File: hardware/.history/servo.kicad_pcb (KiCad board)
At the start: 2 copper layers, 45 x 43 mm, 37 parts, among them J1 servo, J2 Jack-DC, J3 swd, Q2 DMT64M8LSS, SW1 restart, SW2 buzzer, U1 AOZ1284PI, U3 STM32G030F6Px, U4 LDI1117-3.3U-DIO

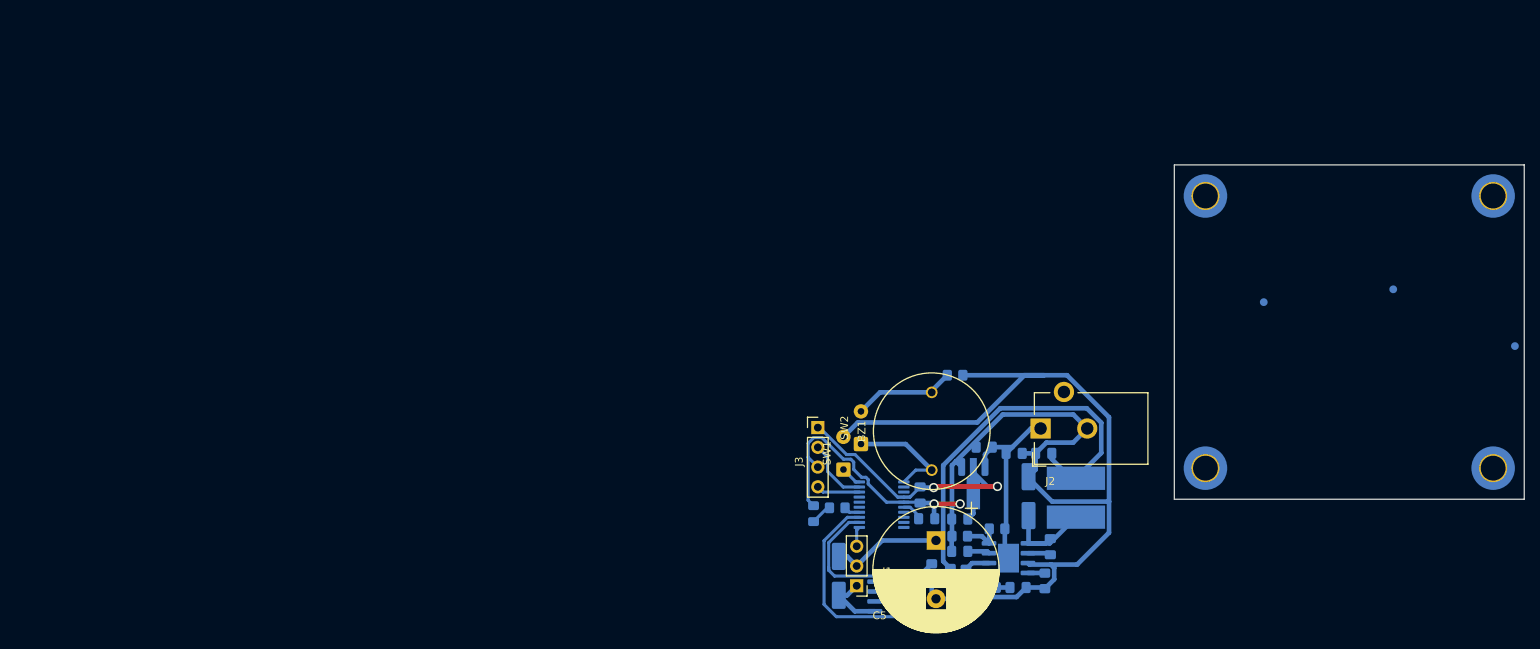
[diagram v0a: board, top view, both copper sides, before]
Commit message: Fix false stall detection after restart
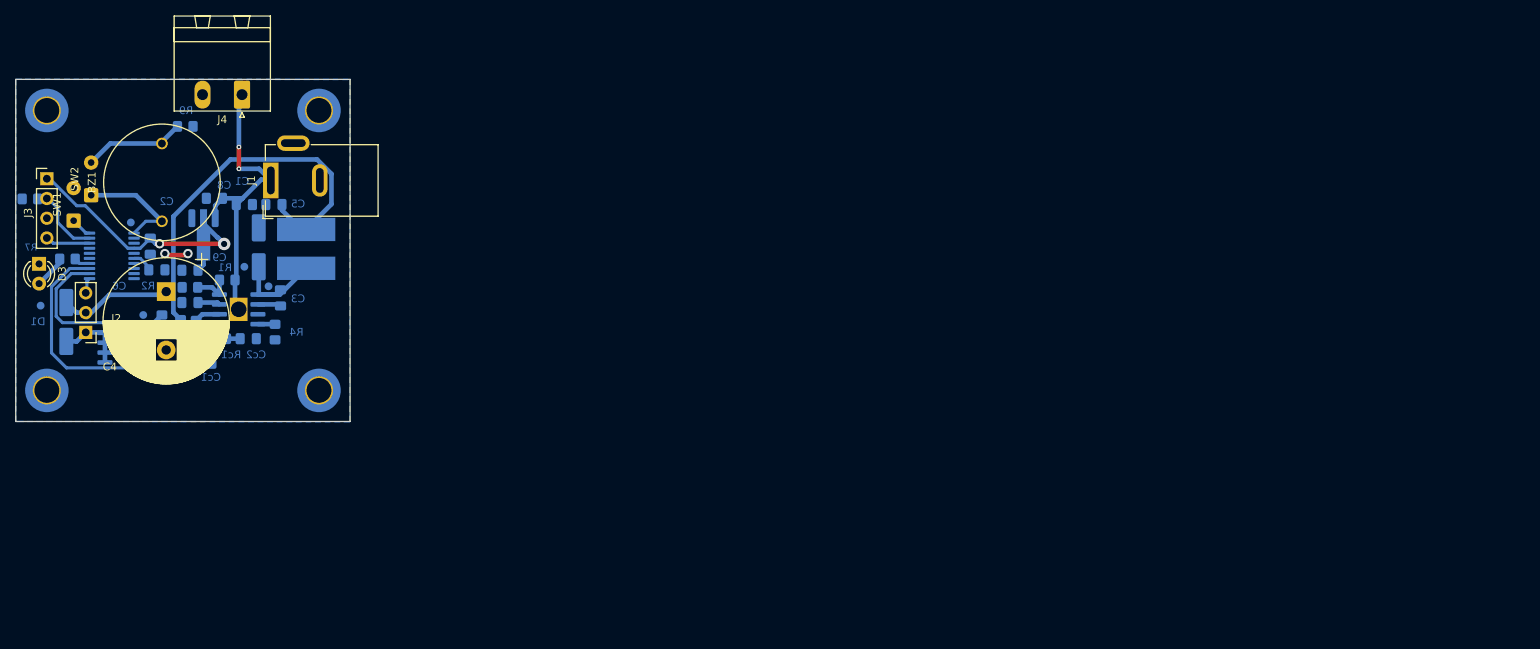
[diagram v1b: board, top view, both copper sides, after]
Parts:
- added Cc1: 150p, Capacitor_SMD:C_0805_2012Metric_Pad1.18x1.45mm_HandSolder, B.Cu at (25.1, 35.6)
- added J4: LED, Connector_Phoenix_MSTB:PhoenixContact_MSTBA_2,5_2-G-5,08_1x02_P5.08mm_Horizontal, F.Cu at (29.1, 1.96)
- added R8: 10k, Resistor_SMD:R_0805_2012Metric_Pad1.20x1.40mm_HandSolder, B.Cu at (1.82, 15.4)
- C7: renamed from C4; value 220n -> 220n 10V
- C8: renamed from C7; value 1u 25V -> 1u 16V
- Cc2: renamed from C6; value 1.5n -> 6.8n
- D3: value KP-2012SURC -> L-7104SURCK; footprint LED_SMD:LED_0805_2012Metric_Pad1.15x1.40mm_HandSolder -> LED_THT:LED_D3.0mm; moved to F.Cu
- J1: renamed from J2; value Jack-DC -> 5.5x2.1; footprint Connector_BarrelJack:BarrelJack_CUI_PJ-102AH_Horizontal -> Connector_BarrelJack:BarrelJack_GCT_DCJ200-10-A_Horizontal
- R9: renamed from R7; value 51k -> 300
- Rc1: renamed from R4; value 10k -> 1M
- U1: footprint Package_SO:SOIC-8-1EP_3.9x4.9mm_P1.27mm_EP2.71x3.7mm -> Package_SO:SOIC-8-1EP_3.9x4.9mm_P1.27mm_EP2.29x3mm_diy
- moved H3 186.3 mm to (4.00, 40.0)
- moved H1 153.1 mm to (39.0, 40.0)
- moved H2 149.4 mm to (4.00, 4.00)
- moved H4 122.9 mm to (39.0, 4.00)
- moved D3 104.7 mm to (3.00, 23.7)
- moved D1 104.6 mm to (6.50, 31.2)
- moved J2 104.4 mm to (9.00, 32.5)
- moved J3 104.2 mm to (4.00, 12.8)
- moved C3 104.0 mm to (34.0, 28.1)
- moved R7 104.0 mm to (6.65, 23.1)
- moved BZ1 104.0 mm to (18.8, 13.3)
- moved C1 104.0 mm to (29.4, 16.1)
- moved C2 104.0 mm to (17.3, 21.5)
- moved C4 104.0 mm to (19.3, 27.3)
- moved C5 104.0 mm to (33.2, 16.1)
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- renumbered C2 to C1, C10 to C2, C1 to C3, C5 to C4, C3 to C5, C9 to C6, C8 to C9, J1 to J2, Q2 to Q1, R8 to R1, R9 to R2, R1 to R3, R2 to R4, R3 to R5, R5 to R6, R6 to R7, U4 to U2
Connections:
- net /mosfet renamed /fet
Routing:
- net GND: track 195.6 -> 4.21 mm
- net +12V: track 25.0 -> 39.2 mm, vias 0 -> 2
- net Net-(D3-A): track 2.79 -> 4.54 mm
- net Net-(D1-A): track 8.28 -> 9.29 mm
- net /fet: track 26.4 -> 27.3 mm
- added copper zone on B.Cu, net GND
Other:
- board size 45 x 43 mm -> 43 x 44 mm
- board text added: "+20mm for dsub?"

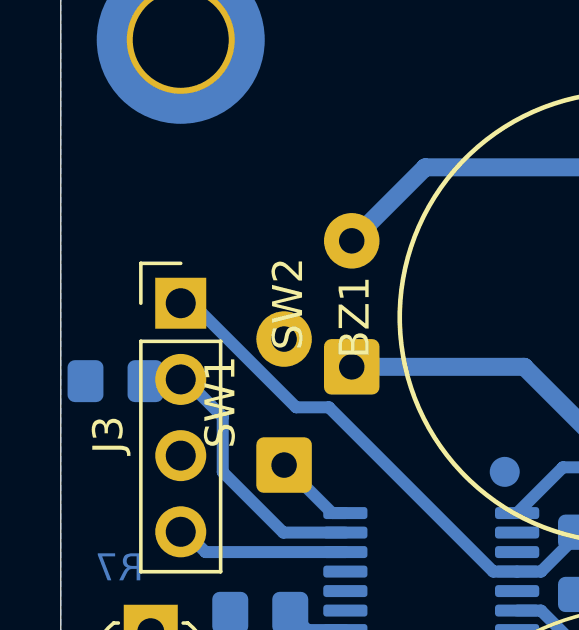
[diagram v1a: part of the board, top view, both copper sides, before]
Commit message: Update PCB for v2
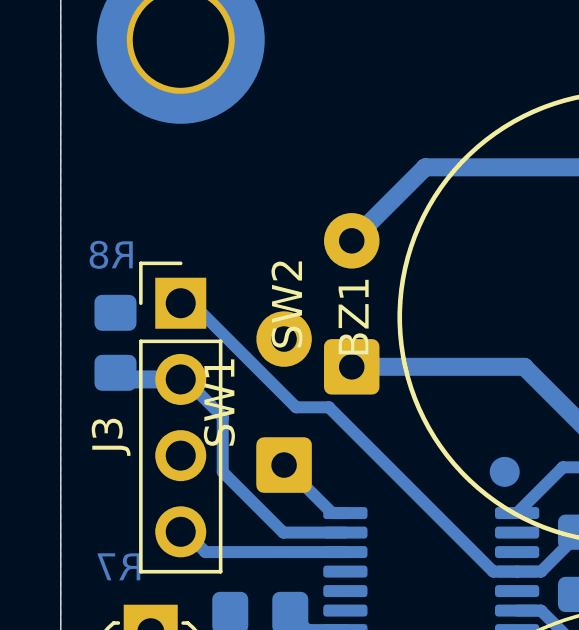
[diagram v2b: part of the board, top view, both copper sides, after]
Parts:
- moved R8 1.28 mm to (1.82, 14.1), turned to 90 degrees
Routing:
- net /swclk: track 8.53 -> 10.8 mm

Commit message: Update PCB
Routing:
- net +5V: track 65.7 -> 67.7 mm
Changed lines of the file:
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@@
 			(net "GND")
 			(pintype "passive")
+			(thermal_bridge_angle 45)
 		)
 		(embedded_fonts no)
@@
 		(tags "capacitor handsolder")
 		(property "Reference" "C2"
-			(at -5.75 -2.1 0)
+			(at -6.450001 -1.500001 0)
 			(layer "B.Cu" knockout)
 			(effects
@@
 	)
 	(segment
-		(start 38.745584 10.300001)
-		(end 40.599999 12.154416)
+		(start 18.949999 27.700001)
+		(end 19.349999 27.300001)
 		(width 0.6)
 		(layer "B.Cu")
@@
 	)
 	(segment
-		(start 18.949999 27.700001)
-		(end 19.349999 27.300001)
+		(start 20.274999 16.525001)
+		(end 27 9.8)
+		(width 0.6)
+		(layer "B.Cu")
+		(net "+5V")
+	)
+	(segment
+		(start 27 9.8)
+		(end 39.4 9.8)
 		(width 0.6)
 		(layer "B.Cu")
@@
 	)
 	(segment
-		(start 20.274999 17.631667)
-		(end 27.606665 10.300001)
+		(start 20.274999 29.975001)
+		(end 20.274999 16.525001)
 		(width 0.6)
 		(layer "B.Cu")
@@
 	)
 	(segment
-		(start 27.606665 10.300001)
-		(end 38.745584 10.300001)
+		(start 40.9 11.3)
+		(end 40.9 15.75)
 		(width 0.6)
 		(layer "B.Cu")
@@
 	)
 	(segment
-		(start 40.599999 12.154416)
-		(end 40.599999 16.050001)
-		(width 0.6)
-		(layer "B.Cu")
-		(net "+5V")
-	)
-	(segment
-		(start 20.274999 29.975001)
-		(end 20.274999 17.631667)
+		(start 40.9 15.75)
+		(end 37.349999 19.300001)
 		(width 0.6)
 		(layer "B.Cu")
@@
 	)
 	(segment
-		(start 40.599999 16.050001)
-		(end 37.349999 19.300001)
+		(start 39.4 9.8)
+		(end 40.9 11.3)
 		(width 0.6)
 		(layer "B.Cu")
@@
 	)
 	(zone
+		(net "+5V")
+		(layer "B.Cu")
+		(hatch none 0.1)
+		(priority 30002)
+		(attr
+			(teardrop
+				(type padvia)
+			)
+		)
+		(connect_pads yes
+			(clearance 0)
+		)
+		(min_thickness 0.0254)
+		(fill yes
+			(island_removal_mode 1)
+		)
+		(polygon
+			(pts
+				(xy 39.769237 17.305027) (xy 39.344973 16.880763) (xy 37.435785 17.800001) (xy 37.349292 19.300708)
+				(xy 40.264212 17.800002)
+			)
+		)
+	)
+	(zone
 		(net "+12V")
 		(layer "B.Cu")
@@
 			)
 		)
-	)
-	(zone
-		(net "+5V")
-		(layer "B.Cu")
-		(hatch none 0.1)
-		(priority 30002)
-		(attr
-			(teardrop
-				(type padvia)
-			)
-		)
-		(connect_pads yes
-			(clearance 0)
-		)
-		(min_thickness 0.0254)
-		(fill yes
-			(island_removal_mode 1)
-		)
-		(polygon
-			(pts
-				(xy 39.769237 17.305027) (xy 39.344973 16.880763) (xy 37.435785 17.800001) (xy 37.349292 19.300708)
-				(xy 40.264212 17.800002)
-			)
-		)

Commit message: Update PCB
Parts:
- moved Cc1 0.80 mm to (25.2, 36.4)
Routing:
- net Net-(U1-COMP): track 2.31 -> 4.37 mm
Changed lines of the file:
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@@
 	(footprint "Capacitor_SMD:C_0805_2012Metric_Pad1.18x1.45mm_HandSolder"
 		(layer "B.Cu")
-		(at 25.1 35.601639 -90)
+		(at 25.2 36.4 -90)
 		(descr "Capacitor SMD 0805 (2012 Metric), square (rectangular) end terminal, IPC_7351 nominal with elongated pad for handsoldering. (Body size source: IPC-SM-782 page 76, https://www.pcb-3d.com/wordpress/wp-content/uploads/ipc-sm-782a_amendment_1_and_2.pdf, https://docs.google.com/spreadsheets/d/1BsfQQcO9C6DZCsRaXUlFlo91Tg2WpOkGARC1WS5S8t0/edit?usp=sharing), generated with kicad-footprint-generator")
 		(tags "capacitor handsolder")
@@
 	)
 	(segment
+		(start 25.099999 35.262499)
+		(end 25.2 35.3625)
+		(width 0.6)
+		(layer "B.Cu")
+		(net "Net-(U1-COMP)")
+	)
+	(segment
 		(start 26.167499 32.282501)
 		(end 25.099999 33.350001)
@@
 	)
 	(segment
+		(start 25.099999 33.350001)
+		(end 25.099999 35.262499)
+		(width 0.6)
+		(layer "B.Cu")
+		(net "Net-(U1-COMP)")
+	)
+	(segment
 		(start 26.167499 31.480001)
 		(end 26.167499 32.282501)
@@
 		(layer "B.Cu")
 		(hatch none 0.1)
-		(priority 30028)
+		(priority 30029)
 		(attr
 			(teardrop
@@
 		(layer "B.Cu")
 		(hatch none 0.1)
-		(priority 30039)
+		(priority 30040)
 		(attr
 			(teardrop
@@
 		(layer "B.Cu")
 		(hatch none 0.1)
-		(priority 30035)
+		(priority 30036)
 		(attr
 			(teardrop
@@
 		(layer "B.Cu")
 		(hatch none 0.1)
-		(priority 30030)
+		(priority 30031)
 		(attr
 			(teardrop
@@
 		(layer "B.Cu")
 		(hatch none 0.1)
-		(priority 30036)
+		(priority 30037)
 		(attr
 			(teardrop
@@
 		(layer "B.Cu")
 		(hatch none 0.1)
-		(priority 30041)
+		(priority 30042)
 		(attr
 			(teardrop
@@
 		(layer "B.Cu")
 		(hatch none 0.1)
-		(priority 30031)
+		(priority 30032)
 		(attr
 			(teardrop
@@
 		(layer "B.Cu")
 		(hatch none 0.1)
-		(priority 30032)
+		(priority 30033)
 		(attr
 			(teardrop
@@
 		(layer "B.Cu")
 		(hatch none 0.1)
-		(priority 30029)
+		(priority 30030)
 		(attr
 			(teardrop
@@
 		(layer "B.Cu")
 		(hatch none 0.1)
-		(priority 30040)
+		(priority 30041)
 		(attr
 			(teardrop
@@
 		(layer "B.Cu")
 		(hatch none 0.1)
-		(priority 30034)
+		(priority 30035)
 		(attr
 			(teardrop
@@
 		(layer "B.Cu")
 		(hatch none 0.1)
-		(priority 30038)
+		(priority 30039)
 		(attr
 			(teardrop
@@
 		(layer "B.Cu")
 		(hatch none 0.1)
-		(priority 30037)
+		(priority 30038)
 		(attr
 			(teardrop
@@
 		(layer "B.Cu")
 		(hatch none 0.1)
-		(priority 30027)
+		(priority 30028)
 		(attr
 			(teardrop
@@
 		(layer "B.Cu")
 		(hatch none 0.1)
-		(priority 30033)
+		(priority 30034)
 		(attr
 			(teardrop
@@
 		(layer "B.Cu")
 		(hatch none 0.1)
-		(priority 30026)
+		(priority 30027)
 		(attr
 			(teardrop
@@
 			)
 		)
+	)
+	(zone
+		(net "Net-(U1-COMP)")
+		(layer "B.Cu")
+		(hatch none 0.1)
+		(priority 30026)
+		(attr
+			(teardrop
+				(type padvia)
+			)
+		)
+		(connect_pads yes
+			(clearance 0)
+		)
+		(min_thickness 0.0254)
+		(fill yes
+			(island_removal_mode 1)
+		)
+		(polygon
+			(pts
+				(xy 24.799999 34.650001) (xy 25.399999 34.650001) (xy 25.680969 33.895672) (xy 25.099999 33.349001)
+				(xy 24.519029 33.895672)
+			)
+		)

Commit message: Change buzzer supply to 12V, update PCB
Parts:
- added Q2: 2N7000, Package_TO_SOT_THT:TO-92_Inline, B.Cu at (15.3, 16.3)
- added R10: 3k, Resistor_SMD:R_0805_2012Metric_Pad1.20x1.40mm_HandSolder, B.Cu at (10.9, 12.7)
- J1: footprint Connector_BarrelJack:BarrelJack_GCT_DCJ200-10-A_Horizontal -> Connector_BarrelJack:BarrelJack_CUI_PJ-102AH_Horizontal
- J4: footprint Connector_Phoenix_MSTB:PhoenixContact_MSTBA_2,5_2-G-5,08_1x02_P5.08mm_Horizontal -> Connector_PinHeader_2.54mm:PinHeader_1x02_P2.54mm_Vertical
- R9: value 300 -> 1k
- moved J4 0.46 mm to (28.7, 2.20), turned to -90 degrees
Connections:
- R9 pad 2: GND -> +12V
- U3 pad 1: Net-(BZ1-+) -> Net-(Q2-G)
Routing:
- net +12V: track 39.2 -> 45.2 mm
- net Net-(BZ1-+): track 14.7 -> 10.5 mm
- net Net-(Q2-G): track 0.00 -> 2.16 mm
- net +5V: track 67.7 -> 67.1 mm
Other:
- board text removed: "+20mm for dsub?"

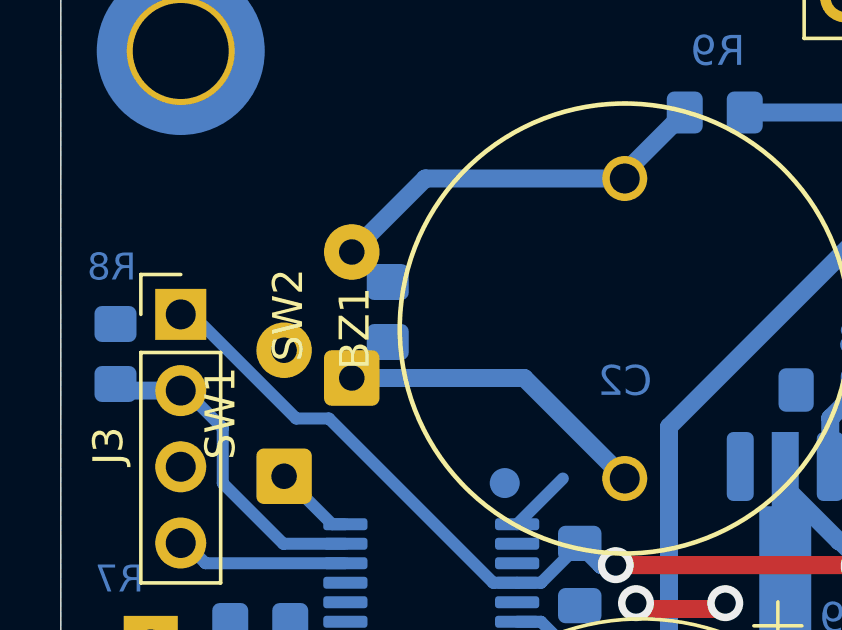
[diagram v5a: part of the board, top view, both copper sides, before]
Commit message: Move footprint for v2
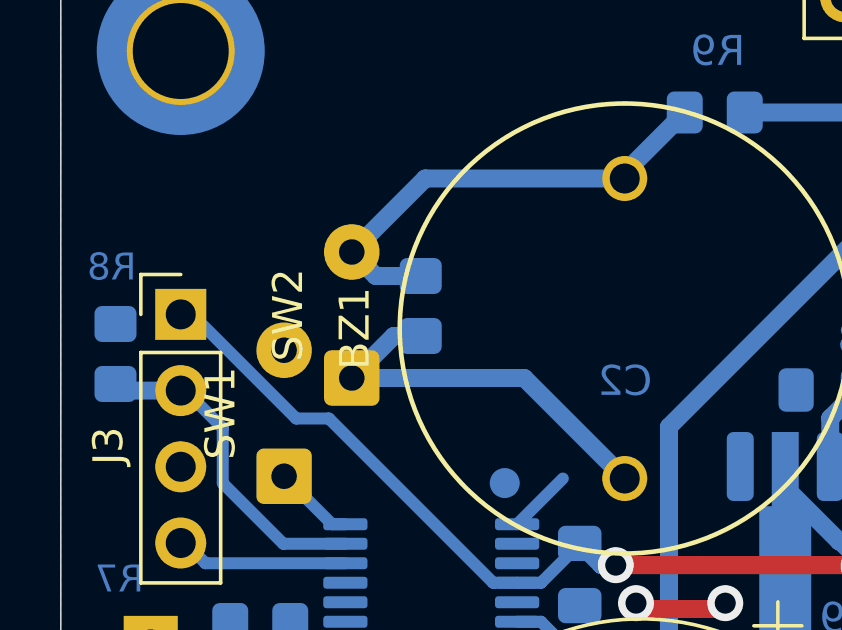
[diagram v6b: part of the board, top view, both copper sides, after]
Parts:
- moved R10 1.12 mm to (12.0, 12.5)
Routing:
- net Net-(BZ1-+): track 10.5 -> 13.4 mm
- net Net-(BZ1--): track 13.1 -> 15.8 mm
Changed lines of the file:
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@@
 	(footprint "Resistor_SMD:R_0805_2012Metric_Pad1.20x1.40mm_HandSolder"
 		(layer "B.Cu")
-		(at 10.9 12.7 90)
+		(at 12 12.5 90)
 		(descr "Resistor SMD 0805 (2012 Metric), square (rectangular) end terminal, IPC-7351 nominal with elongated pad for handsoldering. (Body size source: IPC-SM-782 page 72, https://www.pcb-3d.com/wordpress/wp-content/uploads/ipc-sm-782a_amendment_1_and_2.pdf)")
 		(tags "resistor handsolder")
@@
 	)
 	(segment
+		(start 11.1 13.5)
+		(end 9.699999 14.900001)
+		(width 0.6)
+		(layer "B.Cu")
+		(net "Net-(BZ1-+)")
+	)
+	(segment
 		(start 9.699999 14.900001)
 		(end 15.449999 14.900001)
@@
 	)
 	(segment
+		(start 12 13.5)
+		(end 11.1 13.5)
+		(width 0.6)
+		(layer "B.Cu")
+		(net "Net-(BZ1-+)")
+	)
+	(segment
 		(start 15.449999 14.900001)
 		(end 18.799999 18.250001)
@@
 	)
 	(segment
+		(start 12 11.5)
+		(end 10.499998 11.5)
+		(width 0.6)
+		(layer "B.Cu")
+		(net "Net-(BZ1--)")
+	)
+	(segment
 		(start 9.699999 10.700001)
 		(end 12.149999 8.250001)
@@
 	)
 	(segment
+		(start 10.499998 11.5)
+		(end 9.699999 10.700001)
+		(width 0.6)
+		(layer "B.Cu")
+		(net "Net-(BZ1--)")
+	)
+	(segment
 		(start 18.799999 8.050001)
 		(end 20.799999 6.050001)
@@
 		(layer "B.Cu")
 		(hatch none 0.1)
-		(priority 30005)
+		(priority 30006)
 		(attr
 			(teardrop
@@
 		(layer "B.Cu")
 		(hatch none 0.1)
-		(priority 30014)
+		(priority 30015)
 		(attr
 			(teardrop
@@
 		(layer "B.Cu")
 		(hatch none 0.1)
-		(priority 30006)
+		(priority 30007)
 		(attr
 			(teardrop
@@
 		(layer "B.Cu")
 		(hatch none 0.1)
-		(priority 30010)
+		(priority 30011)
 		(attr
 			(teardrop
@@
 		(layer "B.Cu")
 		(hatch none 0.1)
-		(priority 30011)
+		(priority 30012)
 		(attr
 			(teardrop
@@
 		(layer "B.Cu")
 		(hatch none 0.1)
-		(priority 30015)
+		(priority 30016)
 		(attr
 			(teardrop
@@
 		(layer "B.Cu")
 		(hatch none 0.1)
-		(priority 30012)
+		(priority 30013)
 		(attr
 			(teardrop
@@
 		(layer "B.Cu")
 		(hatch none 0.1)
-		(priority 30009)
+		(priority 30010)
 		(attr
 			(teardrop
@@
 		(layer "B.Cu")
 		(hatch none 0.1)
-		(priority 30008)
+		(priority 30009)
 		(attr
 			(teardrop
@@
 		(layer "B.Cu")
 		(hatch none 0.1)
-		(priority 30004)
+		(priority 30005)
 		(attr
 			(teardrop
@@
 		(layer "B.Cu")
 		(hatch none 0.1)
-		(priority 30007)
+		(priority 30008)
 		(attr
 			(teardrop
@@
 			)
 		)
+	)
+	(zone
+		(net "Net-(BZ1-+)")
+		(layer "B.Cu")
+		(hatch none 0.1)
+		(priority 30004)
+		(attr
+			(teardrop
+				(type padvia)
+			)
+		)
+		(connect_pads yes
+			(clearance 0)
+		)
+		(min_thickness 0.0254)
+		(fill yes
+			(island_removal_mode 1)
+		)
+		(polygon
+			(pts
+				(xy 11.249694 13.8) (xy 11.249694 13.2) (xy 11.1 13.2) (xy 10.887868 13.287868) (xy 9.316851 13.975001)
+				(xy 9.699292 14.900708) (xy 10.624999 15.283149) (xy 11.312132 13.712132) (xy 11.1 13.8)
+			)
+		)
+	)
+	(zone
+		(net "Net-(BZ1-+)")
+		(layer "B.Cu")
+		(hatch none 0.1)
+		(priority 30014)
+		(attr
+			(teardrop
+				(type padvia)
+			)
+		)
+		(connect_pads yes
+			(clearance 0)
+		)
+		(min_thickness 0.0254)
+		(fill yes
+			(island_removal_mode 1)
+		)
+		(polygon
+			(pts
+				(xy 17.954024 16.979762) (xy 17.52976 17.404026) (xy 18.138558 18.603549) (xy 18.803259 18.253261)
+				(xy 19.153547 17.58856)
+			)
+		)
